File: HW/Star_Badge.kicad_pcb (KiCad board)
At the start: 2 copper layers, 180 x 171.6 mm, 55 parts, among them J1 AVR-ISP-6, J2 10118194-0001LF, Q1 Q_NMOS_DGS, Q2 Q_PMOS_DGS, U1 ATTINY861-15XD, U2 TPS613221ADBVT, U3 AP7363-33D-13, X1 Badgelife_sao_connector_v169b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, X2 Badgelife_sao_connector_v169b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, X3 Badgelife_sao_connector_v169b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

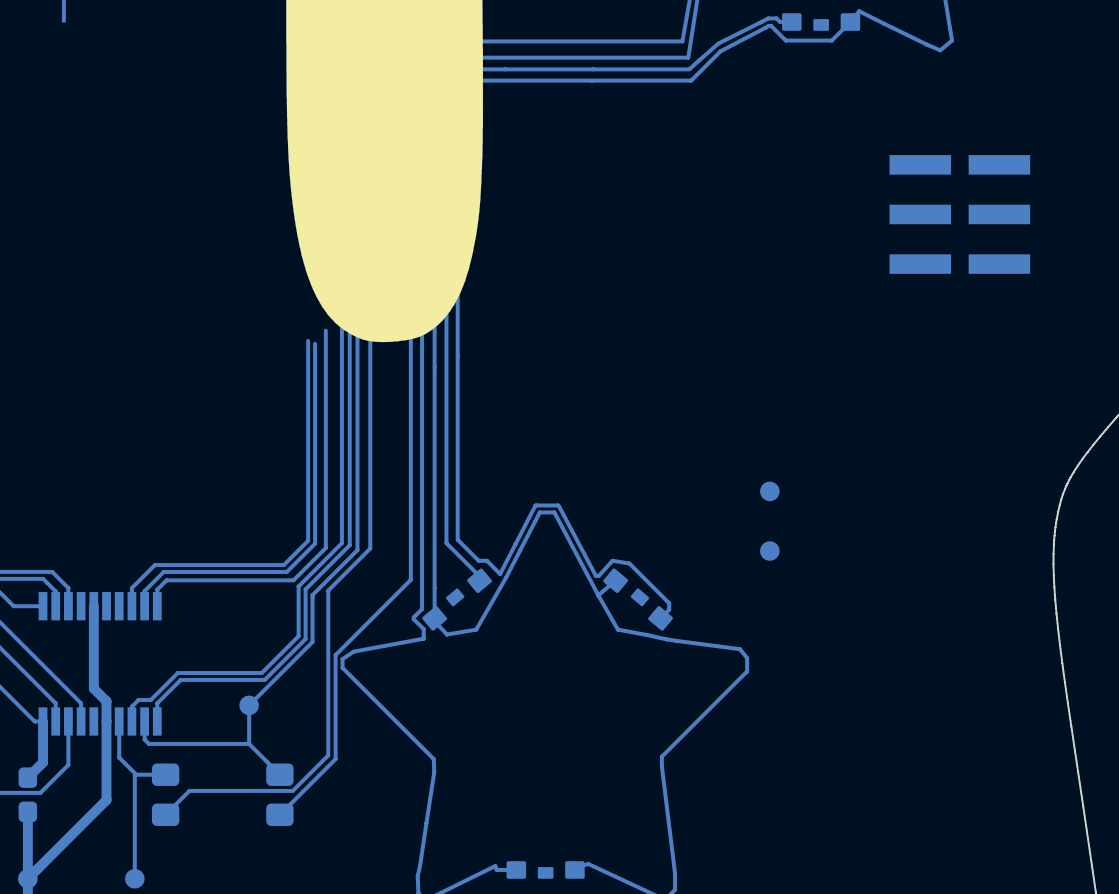
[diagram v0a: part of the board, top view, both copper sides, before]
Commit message: routed miso mosi to programming header
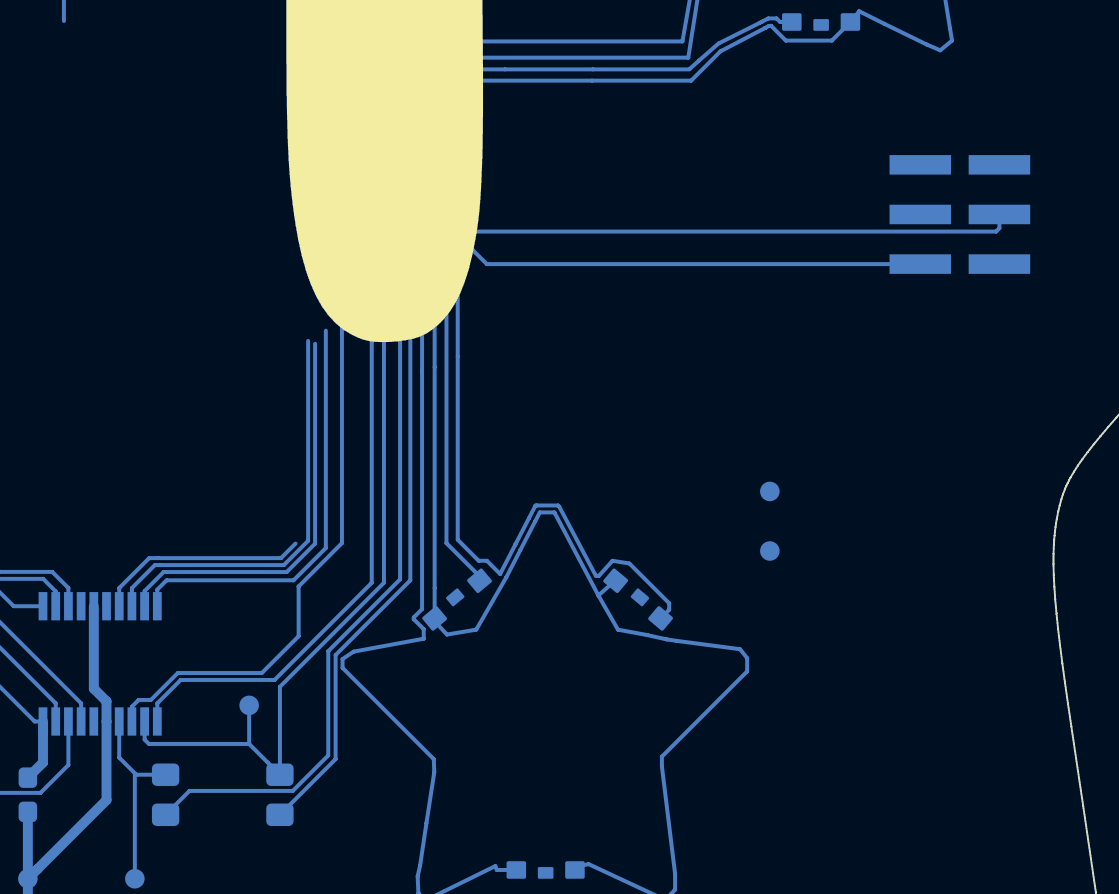
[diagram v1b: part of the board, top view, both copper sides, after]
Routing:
- net /SDA_MOSI: track 27.2 -> 65.3 mm, vias 0 -> 2
- net /R_PWM__MISO: track 32.7 -> 67.7 mm, vias 0 -> 2
- net /EN_RGB0: track 67.3 -> 78.2 mm
- net /G_LED_BUS: track 238.3 -> 242.2 mm, vias 4 -> 6
- net /R_LED_BUS: track 224.0 -> 223.2 mm
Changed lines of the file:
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@@
     (thickness 1.6)
     (drawings 611)
-    (tracks 729)
+    (tracks 757)
     (zones 0)
     (modules 55)
@@
   (via (at 118.3 101.14439) (size 0.4) (drill 0.3) (layers F.Cu B.Cu) (net 6))
   (segment (start 118.3 105.125) (end 118.3 101.14439) (width 0.2032) (layer F.Cu) (net 6))
-  (segment (start 112.05 132.55) (end 115.9 128.7) (width 0.2032) (layer B.Cu) (net 6))
-  (segment (start 115.9 128.7) (end 115.9 112.725) (width 0.2032) (layer B.Cu) (net 6))
-  (segment (start 109.2 140.725) (end 112.05 137.875) (width 0.2032) (layer B.Cu) (net 6))
-  (segment (start 112.05 137.875) (end 112.05 132.55) (width 0.2032) (layer B.Cu) (net 6))
-  (segment (start 115.9 112.725) (end 115.9 112.725) (width 0.2032) (layer B.Cu) (net 6))
-  (via (at 115.9 112.725) (size 0.4) (drill 0.3) (layers F.Cu B.Cu) (net 6))
   (segment (start 118.3 112.75) (end 118.3 105.125) (width 0.2032) (layer B.Cu) (net 6))
-  (via (at 118.3 112.725) (size 0.4) (drill 0.3) (layers F.Cu B.Cu) (net 6))
-  (segment (start 118.3 112.725) (end 115.9 112.725) (width 0.2032) (layer F.Cu) (net 6))
+  (via (at 115.875 113.55) (size 0.4) (drill 0.3) (layers F.Cu B.Cu) (net 6))
+  (segment (start 112.05 132.55) (end 115.875 128.725) (width 0.2032) (layer B.Cu) (net 6))
+  (segment (start 115.875 113.832842) (end 115.875 113.55) (width 0.2032) (layer B.Cu) (net 6))
+  (segment (start 112.05 137.875) (end 112.05 132.55) (width 0.2032) (layer B.Cu) (net 6))
+  (segment (start 115.875 128.725) (end 115.875 113.832842) (width 0.2032) (layer B.Cu) (net 6))
+  (segment (start 109.2 140.725) (end 112.05 137.875) (width 0.2032) (layer B.Cu) (net 6))
+  (via (at 118.3 113.524998) (size 0.4) (drill 0.3) (layers F.Cu B.Cu) (net 6))
+  (segment (start 118.274998 113.55) (end 118.3 113.524998) (width 0.2032) (layer F.Cu) (net 6))
+  (segment (start 115.875 113.55) (end 118.274998 113.55) (width 0.2032) (layer F.Cu) (net 6))
   (segment (start 98.9 56.425887) (end 99.6 55.1) (width 0.2032) (layer B.Cu) (net 11))
   (segment (start 97.4 59.3) (end 98.9 56.425887) (width 0.2032) (layer B.Cu) (net 11))
@@
   (segment (start 117.118794 117.818794) (end 117.118794 129.118794) (width 0.2032) (layer B.Cu) (net 7))
   (segment (start 117.118794 117.818794) (end 117.118794 107.531206) (width 0.2032) (layer B.Cu) (net 7))
-  (segment (start 113.825 127.1) (end 113.825 115.475) (width 0.2032) (layer B.Cu) (net 8))
-  (segment (start 104.57099 139.50401) (end 109.85877 139.50401) (width 0.2032) (layer B.Cu) (net 8))
-  (segment (start 111.675 137.68778) (end 111.675 129.25) (width 0.2032) (layer B.Cu) (net 8))
-  (segment (start 103.35 140.725) (end 104.57099 139.50401) (width 0.2032) (layer B.Cu) (net 8))
-  (segment (start 109.85877 139.50401) (end 111.675 137.68778) (width 0.2032) (layer B.Cu) (net 8))
-  (segment (start 111.675 129.25) (end 113.825 127.1) (width 0.2032) (layer B.Cu) (net 8))
+  (segment (start 102.50802 127.58878) (end 102.955404 127.58878) (width 0.2032) (layer B.Cu) (net 7))
+  (segment (start 100.975 130.05) (end 100.975 129.1218) (width 0.2032) (layer B.Cu) (net 7))
+  (segment (start 100.975 129.1218) (end 102.50802 127.58878) (width 0.2032) (layer B.Cu) (net 7))
+  (segment (start 102.955404 127.58878) (end 109.255404 127.58878) (width 0.2032) (layer B.Cu) (net 7))
+  (segment (start 109.255404 127.58878) (end 110 126.844184) (width 0.2032) (layer B.Cu) (net 7))
   (segment (start 80.845438 127.704562) (end 81.6 126.95) (width 0.2032) (layer B.Cu) (net 8))
   (segment (start 81.6 126.95) (end 81.6 111.1) (width 0.2032) (layer B.Cu) (net 8))
@@
   (segment (start 119.416927 128.516927) (end 117.725 126.825) (width 0.2032) (layer B.Cu) (net 8))
   (via (at 117.725 105.125) (size 0.4) (drill 0.3) (layers F.Cu B.Cu) (net 8))
-  (segment (start 117.725 126.825) (end 117.725 105.125) (width 0.2032) (layer B.Cu) (net 8))
+  (segment (start 117.725 126.825) (end 117.725 114.675) (width 0.2032) (layer B.Cu) (net 8))
   (via (at 117.725 101.975) (size 0.4) (drill 0.3) (layers F.Cu B.Cu) (net 8))
   (segment (start 117.725 101.975) (end 117.725 105.125) (width 0.2032) (layer F.Cu) (net 8))
+  (segment (start 104.57099 139.50401) (end 109.85877 139.50401) (width 0.2032) (layer B.Cu) (net 8))
+  (segment (start 111.675 137.68778) (end 111.675 132.35) (width 0.2032) (layer B.Cu) (net 8))
+  (segment (start 115.35 128.675) (end 115.35 116.25) (width 0.2032) (layer B.Cu) (net 8))
+  (segment (start 111.675 132.35) (end 115.35 128.675) (width 0.2032) (layer B.Cu) (net 8))
+  (segment (start 103.35 140.725) (end 104.57099 139.50401) (width 0.2032) (layer B.Cu) (net 8))
+  (segment (start 109.85877 139.50401) (end 111.675 137.68778) (width 0.2032) (layer B.Cu) (net 8))
+  (segment (start 115.35 115.05) (end 115.35 115.05) (width 0.2032) (layer B.Cu) (net 8))
+  (via (at 115.35 114.65) (size 0.4) (drill 0.3) (layers F.Cu B.Cu) (net 8))
+  (segment (start 115.35 115.2) (end 115.35 115.05) (width 0.2032) (layer B.Cu) (net 8))
+  (segment (start 115.35 115.2) (end 115.35 114.65) (width 0.2032) (layer B.Cu) (net 8))
+  (segment (start 115.35 116.25) (end 115.35 115.2) (width 0.2032) (layer B.Cu) (net 8))
+  (segment (start 117.725 114.675) (end 117.725 105.125) (width 0.2032) (layer B.Cu) (net 8))
+  (via (at 117.725 114.65) (size 0.4) (drill 0.3) (layers F.Cu B.Cu) (net 8))
+  (segment (start 117.725 114.65) (end 115.35 114.65) (width 0.2032) (layer F.Cu) (net 8))
   (segment (start 86.225 131.725) (end 85.575 131.075) (width 0.2032) (layer B.Cu) (net 9))
   (segment (start 87.125 131.875) (end 86.225 131.725) (width 0.2032) (layer B.Cu) (net 9))
@@
   (segment (start 102.275 136.8782) (end 102.4968 137.1) (width 0.2032) (layer B.Cu) (net 14))
   (segment (start 107.625 137.1) (end 107.625 135.125) (width 0.2032) (layer B.Cu) (net 14))
-  (segment (start 107.625 135.125) (end 110.86939 131.88061) (width 0.2032) (layer B.Cu) (net 14))
-  (segment (start 110.86939 129.48061) (end 113.16939 127.18061) (width 0.2032) (layer B.Cu) (net 14))
-  (segment (start 110.86939 129.60561) (end 110.86939 129.48061) (width 0.2032) (layer B.Cu) (net 14))
-  (segment (start 110.86939 131.88061) (end 110.86939 129.60561) (width 0.2032) (layer B.Cu) (net 14))
-  (segment (start 113.16939 127.18061) (end 113.16939 115.31939) (width 0.2032) (layer B.Cu) (net 14))
+  (via (at 118.875 111.625) (size 0.4) (drill 0.3) (layers F.Cu B.Cu) (net 14))
+  (segment (start 119.79 112.54) (end 119.074999 111.824999) (width 0.2032) (layer B.Cu) (net 14))
+  (segment (start 119.074999 111.824999) (end 118.875 111.625) (width 0.2032) (layer B.Cu) (net 14))
+  (segment (start 141.975 112.54) (end 119.79 112.54) (width 0.2032) (layer B.Cu) (net 14))
+  (via (at 114.525 111.599998) (size 0.4) (drill 0.3) (layers F.Cu B.Cu) (net 14))
+  (segment (start 114.525 128.85) (end 114.525 111.88284) (width 0.2032) (layer B.Cu) (net 14))
+  (segment (start 114.550002 111.625) (end 114.525 111.599998) (width 0.2032) (layer F.Cu) (net 14))
+  (segment (start 114.525 111.88284) (end 114.525 111.599998) (width 0.2032) (layer B.Cu) (net 14))
+  (segment (start 109.2 134.175) (end 114.525 128.85) (width 0.2032) (layer B.Cu) (net 14))
+  (segment (start 109.2 138.675) (end 109.2 134.175) (width 0.2032) (layer B.Cu) (net 14))
+  (segment (start 118.625 111.625) (end 118.875 111.625) (width 0.2032) (layer F.Cu) (net 14))
+  (segment (start 118.625 111.625) (end 114.550002 111.625) (width 0.2032) (layer F.Cu) (net 14))
   (segment (start 102.6572 147.75) (end 106.45 147.75) (width 0.508) (layer B.Cu) (net 15))
   (segment (start 102.6572 147.75) (end 96.3 147.75) (width 0.508) (layer B.Cu) (net 15))
@@
   (segment (start 102.925 135.0218) (end 104.1218 133.825) (width 0.2032) (layer B.Cu) (net 17))
   (segment (start 102.925 135.95) (end 102.925 135.0218) (width 0.2032) (layer B.Cu) (net 17))
-  (segment (start 104.1218 133.825) (end 108.422092 133.825) (width 0.2032) (layer B.Cu) (net 17))
-  (segment (start 110.51378 129.18622) (end 112.775 126.925) (width 0.2032) (layer B.Cu) (net 17))
-  (segment (start 108.422092 133.825) (end 110.51378 131.733312) (width 0.2032) (layer B.Cu) (net 17))
-  (segment (start 110.51378 131.733312) (end 110.51378 129.18622) (width 0.2032) (layer B.Cu) (net 17))
-  (segment (start 112.775 126.925) (end 112.775 115.375) (width 0.2032) (layer B.Cu) (net 17))
+  (segment (start 104.1218 133.825) (end 108.925 133.825) (width 0.2032) (layer B.Cu) (net 17))
+  (segment (start 108.925 133.825) (end 113.9 128.85) (width 0.2032) (layer B.Cu) (net 17))
+  (segment (start 113.9 128.85) (end 113.9 116.5) (width 0.2032) (layer B.Cu) (net 17))
+  (segment (start 113.9 116.5) (end 113.9 110.875) (width 0.2032) (layer B.Cu) (net 17))
+  (segment (start 113.9 110.875) (end 113.9 110.875) (width 0.2032) (layer B.Cu) (net 17))
+  (via (at 113.9 110.875) (size 0.4) (drill 0.3) (layers F.Cu B.Cu) (net 17))
+  (segment (start 113.9 110.875) (end 118.9 110.875) (width 0.2032) (layer F.Cu) (net 17))
+  (segment (start 118.9 110.875) (end 118.9 110.875) (width 0.2032) (layer F.Cu) (net 17))
+  (via (at 118.9 110.875) (size 0.4) (drill 0.3) (layers F.Cu B.Cu) (net 17))
+  (segment (start 146.025 110.7032) (end 146.025 110) (width 0.2032) (layer B.Cu) (net 17))
+  (segment (start 145.8532 110.875) (end 146.025 110.7032) (width 0.2032) (layer B.Cu) (net 17))
+  (segment (start 118.9 110.875) (end 145.8532 110.875) (width 0.2032) (layer B.Cu) (net 17))
   (segment (start 97.075 138.05) (end 96.3 138.825) (width 0.508) (layer B.Cu) (net 18))
   (segment (start 97.075 135.95) (end 97.075 138.05) (width 0.508) (layer B.Cu) (net 18))
